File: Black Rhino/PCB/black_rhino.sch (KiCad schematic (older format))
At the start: 166 parts, among them SW1 SW_Push, U1 ATmega32U4-AU, Y1 16MHz

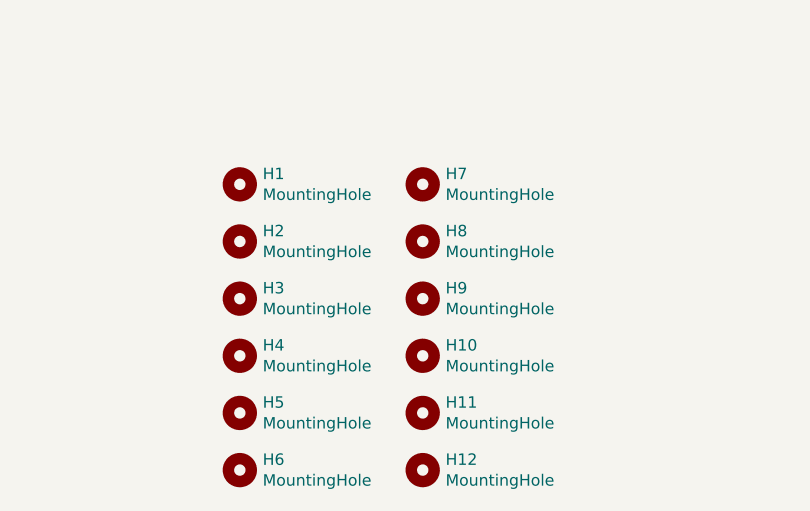
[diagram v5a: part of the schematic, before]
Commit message: Add Black Rhino-Base & Improve Black Rhino-PCB
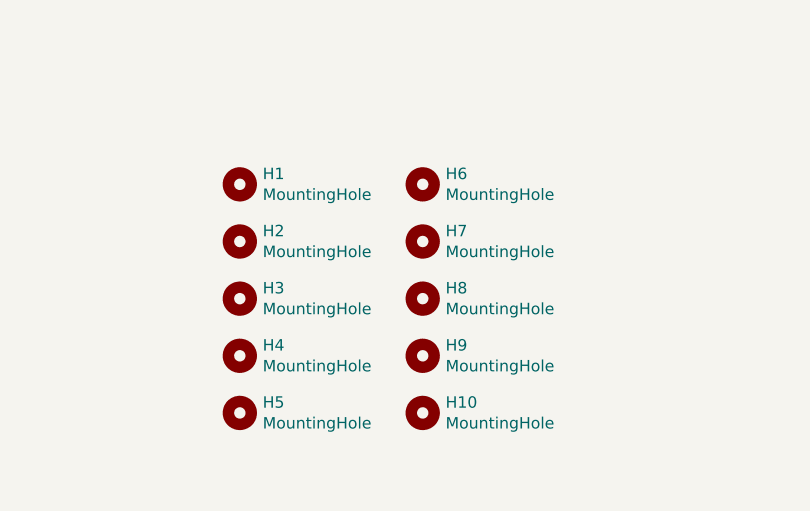
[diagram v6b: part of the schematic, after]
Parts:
- removed H11, H12: MountingHole, MountingHole:MountingHole_2mm, symbol Mechanical:MountingHole
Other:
- moved on the sheet: H10, H6, H7, H8, H9
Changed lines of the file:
@@
 L Mechanical:MountingHole H6
 U 1 1 5F297D56
-P 4400 14100
-F 0 "H6" H 4500 14146 50  0000 L CNN
-F 1 "MountingHole" H 4500 14055 50  0000 L CNN
-F 2 "MountingHole:MountingHole_2mm" H 4400 14100 50  0001 C CNN
-F 3 "~" H 4400 14100 50  0001 C CNN
-	1    4400 14100
-	1    0    0    -1
-$EndComp
-$Comp
-L Mechanical:MountingHole H7
-U 1 1 5F2A8030
 P 5200 12850
-F 0 "H7" H 5300 12896 50  0000 L CNN
+F 0 "H6" H 5300 12896 50  0000 L CNN
 F 1 "MountingHole" H 5300 12805 50  0000 L CNN
 F 2 "MountingHole:MountingHole_2mm" H 5200 12850 50  0001 C CNN
@@
 $EndComp
 $Comp
-L Mechanical:MountingHole H8
-U 1 1 5F2B82E0
+L Mechanical:MountingHole H7
+U 1 1 5F2A8030
 P 5200 13100
-F 0 "H8" H 5300 13146 50  0000 L CNN
+F 0 "H7" H 5300 13146 50  0000 L CNN
 F 1 "MountingHole" H 5300 13055 50  0000 L CNN
 F 2 "MountingHole:MountingHole_2mm" H 5200 13100 50  0001 C CNN
@@
 $EndComp
 $Comp
-L Mechanical:MountingHole H9
-U 1 1 5F316618
+L Mechanical:MountingHole H8
+U 1 1 5F2B82E0
 P 5200 13350
-F 0 "H9" H 5300 13396 50  0000 L CNN
+F 0 "H8" H 5300 13396 50  0000 L CNN
 F 1 "MountingHole" H 5300 13305 50  0000 L CNN
 F 2 "MountingHole:MountingHole_2mm" H 5200 13350 50  0001 C CNN
@@
 $EndComp
 $Comp
-L Mechanical:MountingHole H10
-U 1 1 5F31661E
+L Mechanical:MountingHole H9
+U 1 1 5F316618
 P 5200 13600
-F 0 "H10" H 5300 13646 50  0000 L CNN
+F 0 "H9" H 5300 13646 50  0000 L CNN
 F 1 "MountingHole" H 5300 13555 50  0000 L CNN
 F 2 "MountingHole:MountingHole_2mm" H 5200 13600 50  0001 C CNN
@@
 $EndComp
 $Comp
-L Mechanical:MountingHole H11
-U 1 1 5F316624
+L Mechanical:MountingHole H10
+U 1 1 5F31661E
 P 5200 13850
-F 0 "H11" H 5300 13896 50  0000 L CNN
+F 0 "H10" H 5300 13896 50  0000 L CNN
 F 1 "MountingHole" H 5300 13805 50  0000 L CNN
 F 2 "MountingHole:MountingHole_2mm" H 5200 13850 50  0001 C CNN
@@
 	1    0    0    -1
 $EndComp
-$Comp
-L Mechanical:MountingHole H12
-U 1 1 5F31662A
-P 5200 14100
-F 0 "H12" H 5300 14146 50  0000 L CNN
-F 1 "MountingHole" H 5300 14055 50  0000 L CNN
-F 2 "MountingHole:MountingHole_2mm" H 5200 14100 50  0001 C CNN
-F 3 "~" H 5200 14100 50  0001 C CNN
-	1    5200 14100
-	1    0    0    -1
-$EndComp
